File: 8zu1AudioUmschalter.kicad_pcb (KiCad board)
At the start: 2 copper layers, 59 x 65 mm, 63 parts, among them IC1 ATMEGA8A-A, IC2 MAX9890, IC3 TMP75, J1 USB, J2 LUM 1503-07, J3 LUM 1503-07, J4 LUM 1503-07, J5 LUM 1503-07, J6 LUM 1503-07, J7 LUM 1503-07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

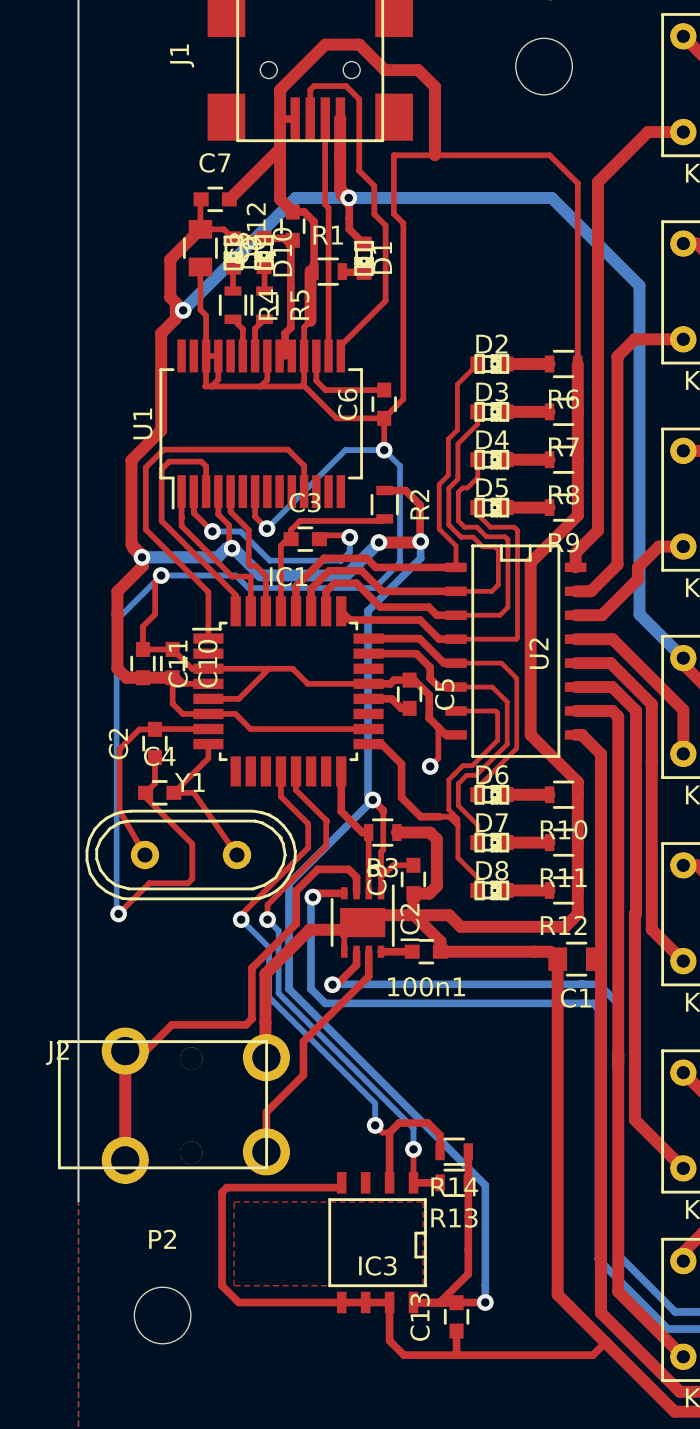
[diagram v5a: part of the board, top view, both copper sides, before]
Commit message: Via Bohrdurchmesser angepasst
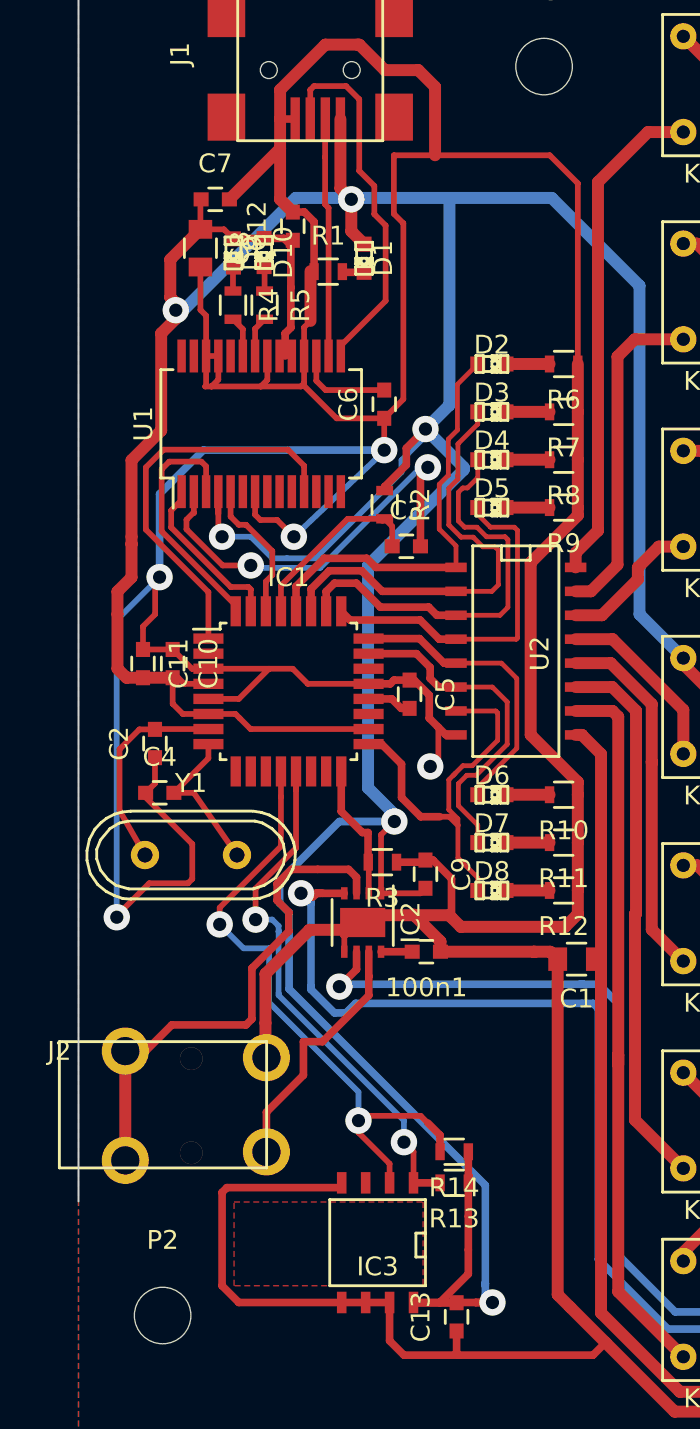
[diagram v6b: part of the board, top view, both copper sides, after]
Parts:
- moved C3 5.38 mm to (150.4, 92.2)
- moved R3 1.57 mm to (149.1, 109.0)
- moved C9 0.70 mm to (151.4, 109.6), turned to 270 degrees
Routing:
- net VCC: track 348.2 -> 365.6 mm, vias 8 -> 6
- net /DTR: track 13.3 -> 22.6 mm
- net GND: track 423.4 -> 420.3 mm
- net /SCL: track 31.4 -> 33.9 mm
- net /CH_L_REL_IN: track 121.1 -> 123.3 mm
- net Net-(IC2-Pad3): track 25.7 -> 27.0 mm
- net /SDA: track 28.5 -> 29.7 mm
- net Net-(IC2-Pad7): track 12.9 -> 13.5 mm
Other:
- net class Default: via_dia 0.889 -> 1.4; via_drill 0.635 -> 0.8
- rule via_min_drill: 0.508 -> 0.8
- rule via_min_size: 0.889 -> 1.4

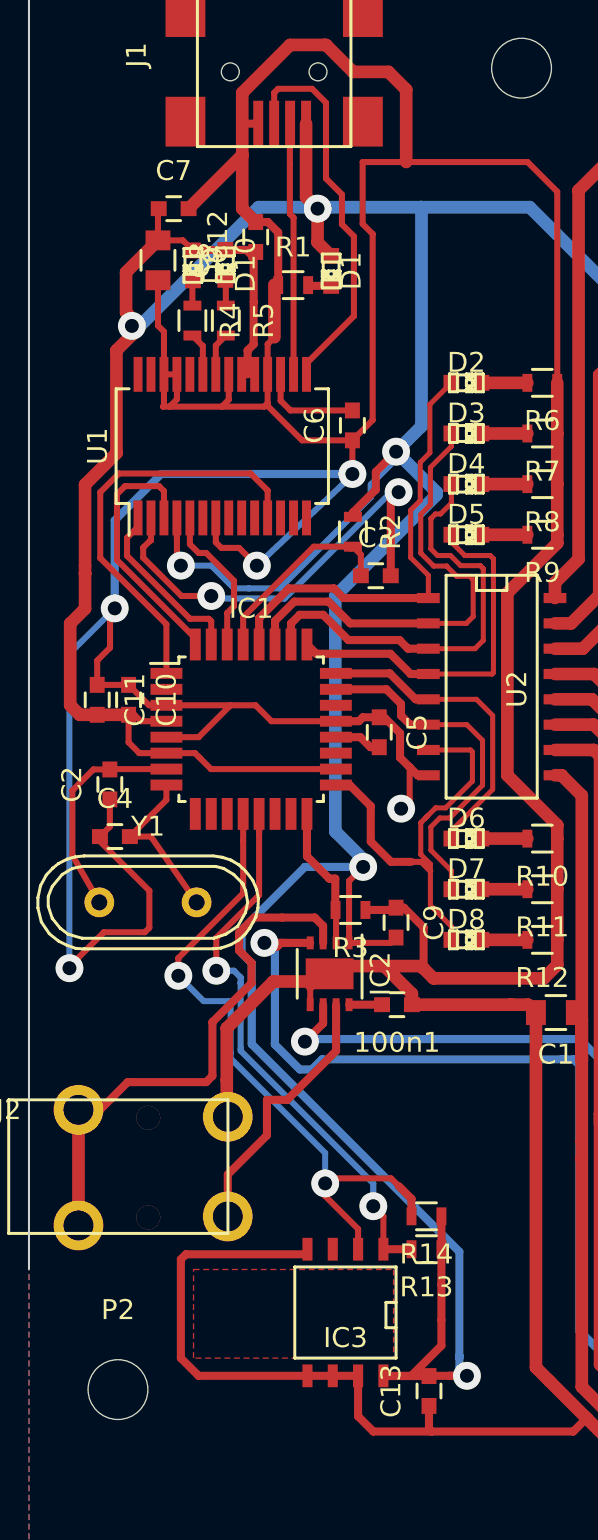
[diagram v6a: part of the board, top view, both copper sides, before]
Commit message: Direkte Leiterbahnen zwischen Pads entfernt
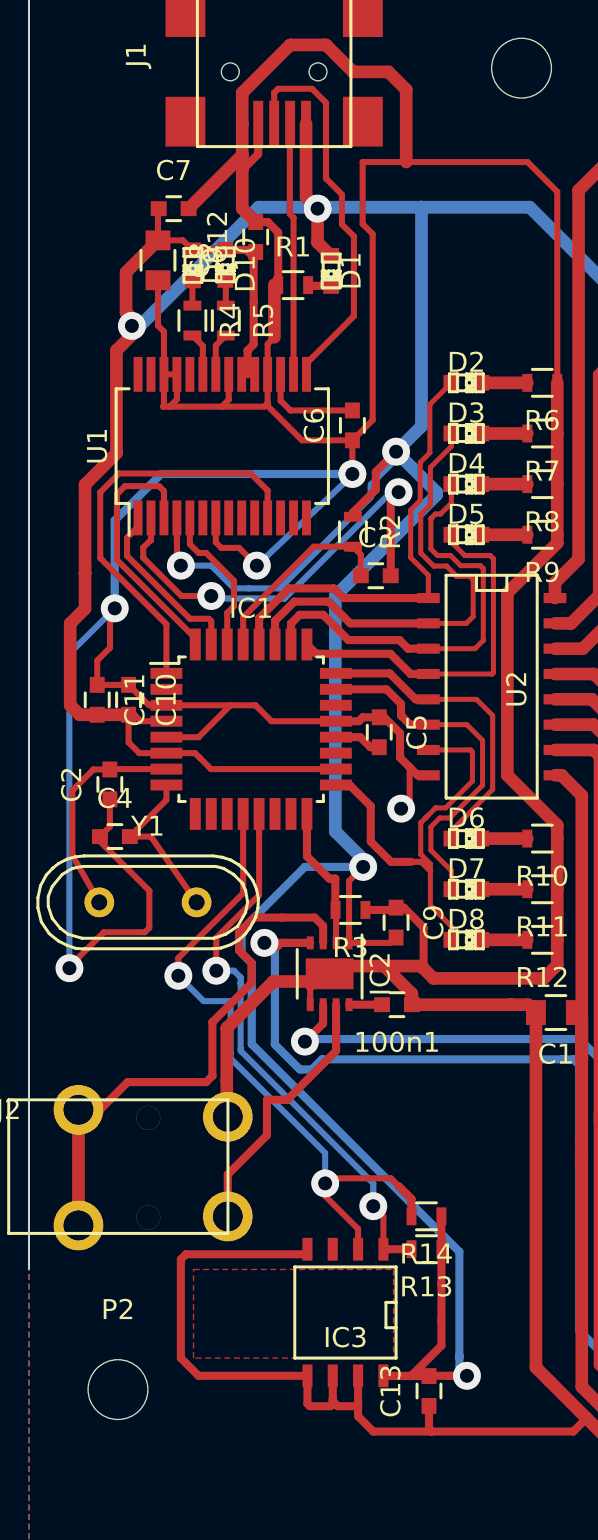
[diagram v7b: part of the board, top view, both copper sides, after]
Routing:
- net GND: track 420.3 -> 425.5 mm

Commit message: Text in Kupferlage dazugefügt, damit man richtig fertigen kann.
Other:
- board text added: "BACK"
- board text added: "FRONT"
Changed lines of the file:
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@@
-(kicad_pcb (version 4) (host pcbnew "(2015-03-12 BZR 5508)-product")
+(kicad_pcb (version 4) (host pcbnew "(2014-08-05 BZR 5054)-product")
   (general
     (links 172)
@@
     (area 130.851857 61.225059 220 152.7)
     (thickness 1.6)
-    (drawings 5)
+    (drawings 7)
     (tracks 809)
     (zones 0)
@@
   )
   (setup
-    (last_trace_width 0.4064)
+    (last_trace_width 0.254)
     (user_trace_width 0.254)
     (user_trace_width 0.3048)
@@
     (visible_elements 7FFFFFFF)
     (pcbplotparams
-      (layerselection 0x00030_80000001)
+      (layerselection 0x00000_80000001)
       (usegerberextensions false)
       (excludeedgelayer true)
@@
       (padsonsilk false)
       (subtractmaskfromsilk false)
-      (outputformat 1)
+      (outputformat 2)
       (mirror false)
       (drillshape 1)
       (scaleselection 1)
-      (outputdirectory ""))
+      (outputdirectory gerber/))
   )
   (net 0 "")
@@
     (model SMD_Packages.3dshapes/SOIC-8-N.wrl
       (at (xyz 0 0 0))
-      (scale (xyz 0.5 0.38 0.5))
+      (scale (xyz 0.5 0.3799999952316284 0.5))
       (rotate (xyz 0 0 0))
     )
@@
     (model SMD_Packages.3dshapes/SO-16-N.wrl
       (at (xyz 0 0 0))
-      (scale (xyz 0.5 0.4 0.5))
+      (scale (xyz 0.5 0.4000000059604645 0.5))
       (rotate (xyz 0 0 0))
     )
@@
     (pad "" thru_hole circle (at 7 5.9) (size 1.2 1.2) (drill 1.2) (layers *.Cu *.Mask F.SilkS))
   )
+  (gr_text BACK (at 152.4 139.4) (layer B.Cu)
+    (effects (font (size 1.5 1.5) (thickness 0.3)) (justify mirror))
+  )
+  (gr_text FRONT (at 152.4 139.4) (layer F.Cu)
+    (effects (font (size 1.5 1.5) (thickness 0.3) italic))
+  )
   (dimension 59 (width 0.3) (layer Dwgs.User)
     (gr_text "59,000 mm" (at 162.5 151.349999) (layer Dwgs.User)
@@
     (min_thickness 0.2)
     (keepout (tracks allowed) (vias allowed) (copperpour not_allowed))
-    (fill (arc_segments 16) (thermal_gap 0.35) (thermal_bridge_width 0.35))
+    (fill yes (arc_segments 16) (thermal_gap 0.35) (thermal_bridge_width 0.35))
     (polygon
       (pts
